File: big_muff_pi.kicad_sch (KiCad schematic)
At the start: 63 parts, among them J1 NMJ6HHD2, J2 NMJ6HHD2, Q1 MMBT5551, Q2 MMBT5551, Q3 MMBT5551, Q4 MMBT5551, Q5 MMBT5551, SW1 SW_DPDT_x2

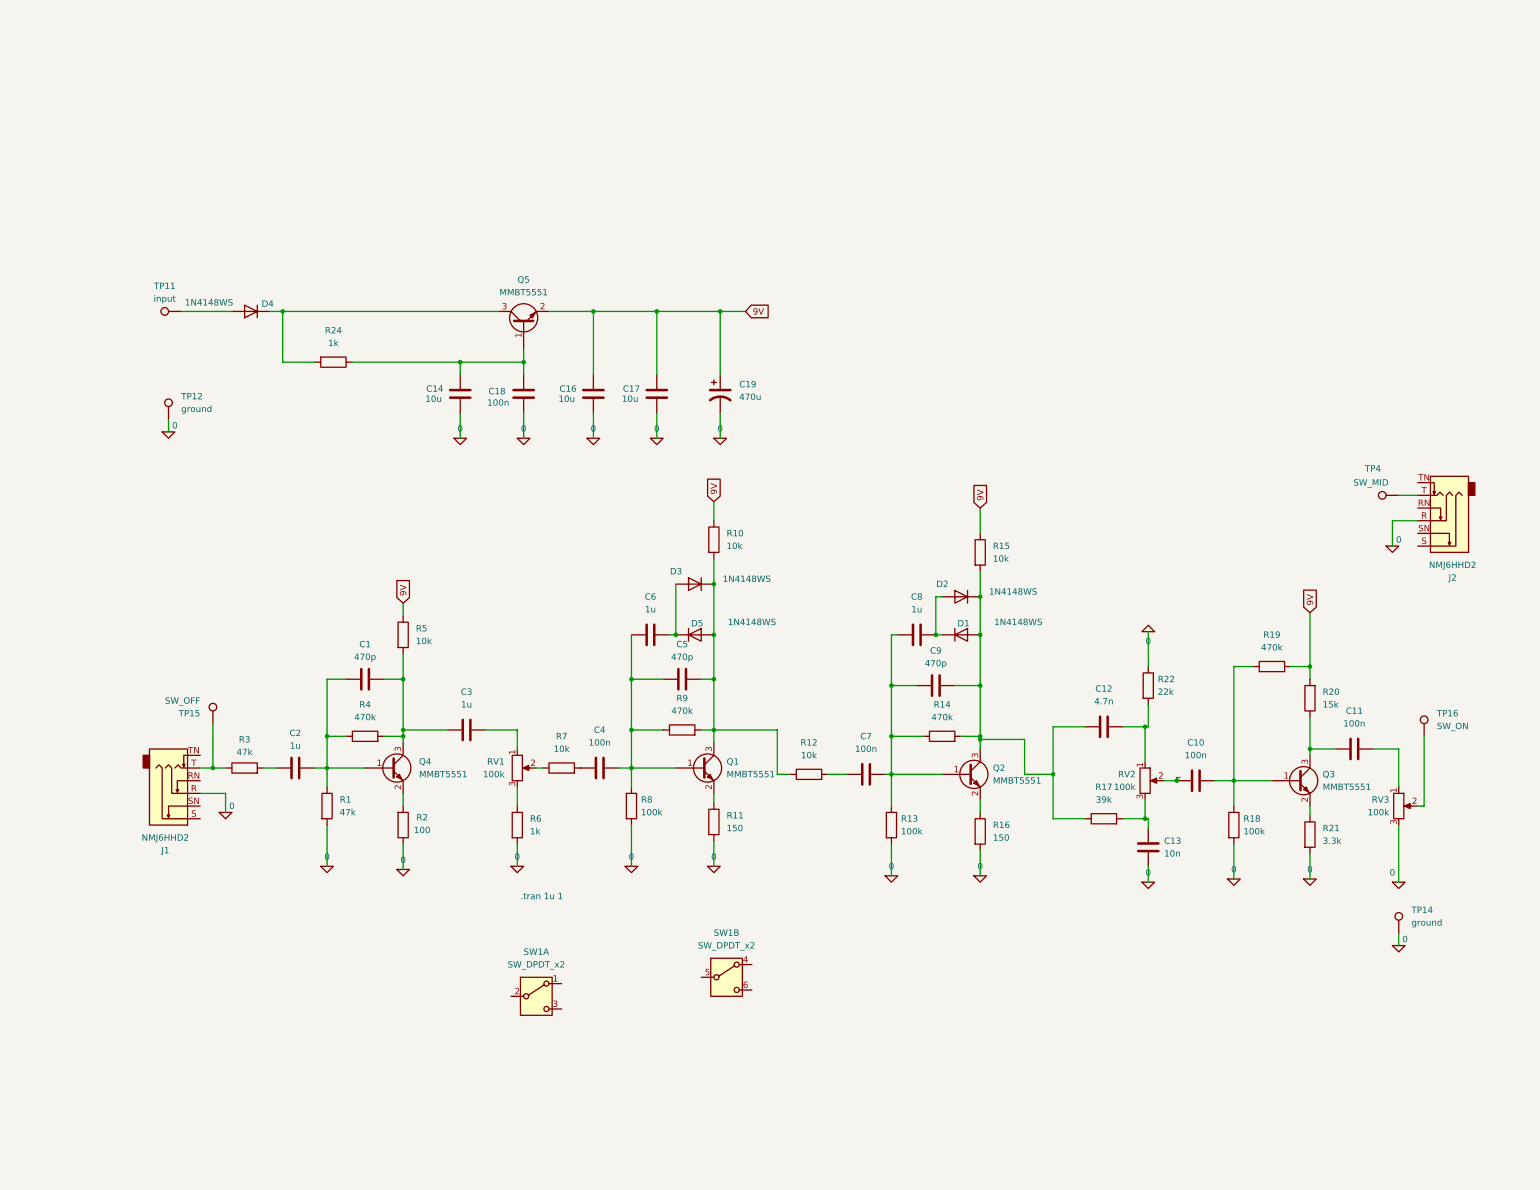
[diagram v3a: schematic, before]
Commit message: 3D bodies
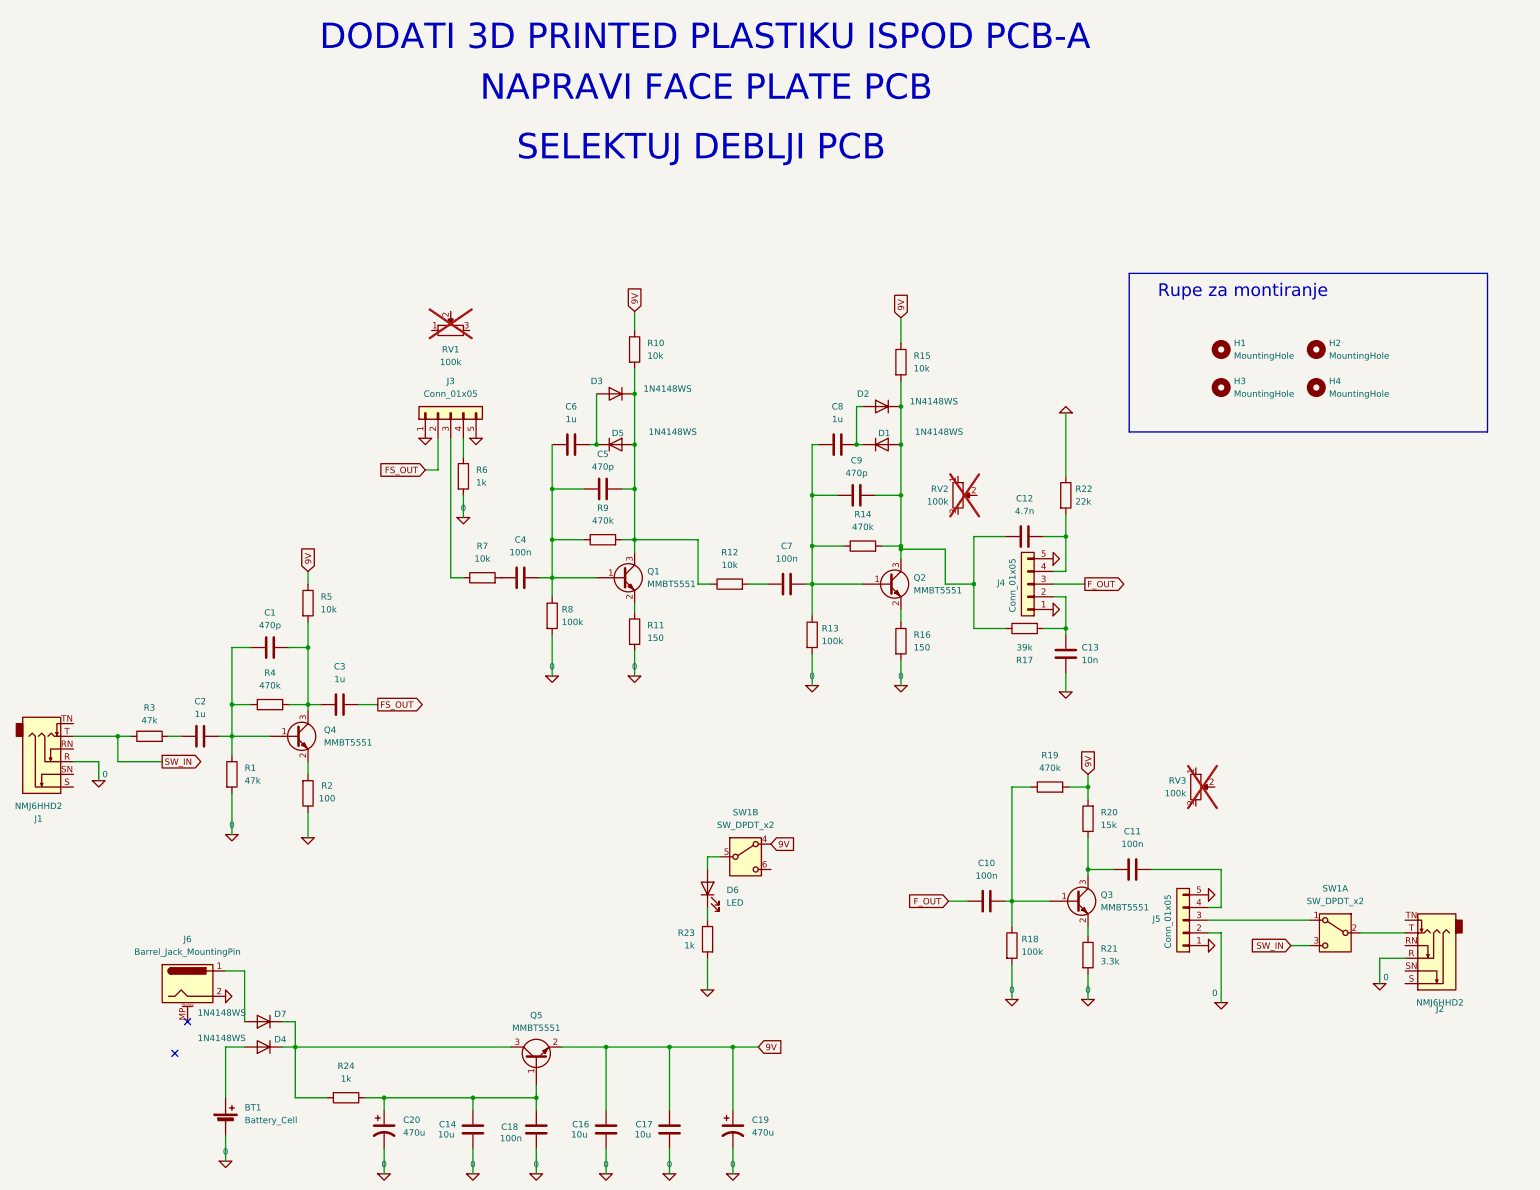
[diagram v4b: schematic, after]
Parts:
- removed TP11: input, TestPoint:TestPoint_THTPad_2.5x2.5mm_Drill1.2mm, symbol Connector:TestPoint
- removed TP12, TP14: ground, TestPoint:TestPoint_THTPad_2.5x2.5mm_Drill1.2mm, symbol Connector:TestPoint
- removed TP15: SW_OFF, TestPoint:TestPoint_THTPad_2.5x2.5mm_Drill1.2mm, symbol Connector:TestPoint
- removed TP16: SW_ON, TestPoint:TestPoint_THTPad_2.5x2.5mm_Drill1.2mm, symbol Connector:TestPoint
- removed TP4: SW_MID, TestPoint:TestPoint_THTPad_2.5x2.5mm_Drill1.2mm, symbol Connector:TestPoint
- added BT1: Battery_Cell, pedale:BatteryHolder_Eagle_12BH611-GR, symbol Device:Battery_Cell
- added C20: 470u, Capacitor_THT:CP_Radial_D8.0mm_P3.50mm, symbol Device:C_Polarized_US
- added D6: LED, LED_THT:LED_D5.0mm, symbol Device:LED
- added D7: 1N4148WS, Diode_SMD:D_SOD-323, symbol Diode:1N4148WS
- added H1, H2, H3, H4: MountingHole, pedale:M3_hole_with_spacer, symbol Mechanical:MountingHole
- added J3, J4, J5: Conn_01x05, Connector_JST:JST_EH_B5B-EH-A_1x05_P2.50mm_Vertical, symbol Connector_Generic:Conn_01x05
- added J6: Barrel_Jack_MountingPin, Connector_BarrelJack:BarrelJack_GCT_DCJ200-10-A_Horizontal, symbol Connector:Barrel_Jack_MountingPin
- added R23: 1k, Resistor_SMD:R_0603_1608Metric_Pad0.98x0.95mm_HandSolder, symbol Device:R
- RV1, RV2, RV3: now not fitted
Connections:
- net 0: now also BT1.2 (-), C20.2, J3.1 (Pin_1), J3.5 (Pin_5), J4.1 (Pin_1), J4.5 (Pin_5), J5.1 (Pin_1), J5.2 (Pin_2), J5.5 (Pin_5), J6.2, R23.2; no longer RV3.3
- net 9V: now also SW1.4 (A)
- net at D4.1 (K), Q5.3 (C), R24.2: now also D7.1 (K)
- net at D4.2 (A): now also BT1.1 (+)
- net at C12.2, R22.2: now also J4.4 (Pin_4); no longer RV2.1
- net at C14.1, C18.2, Q5.1 (B)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: now also C20.1
- net SW_IN: now reaches J1.T, R3.1
- net SW_IN: now also SW1.3 (C)
- net at C13.2, R17.2: now also J4.2 (Pin_2); no longer RV2.3
- net at RV1.1: no longer C3.2
- net at R7.1: now also J3.3 (Pin_3); no longer RV1.2
- net at R6.1: now also J3.4 (Pin_4); no longer RV1.3
- net at J2.T: now also SW1.2 (B)
- net at RV2.2: no longer C10.1
- net at RV3.1: no longer C11.2
- net at SW1.1 (A): now also J5.3 (Pin_3)
- net at SW1.5 (B): now also D6.2 (A)
- new net: D6.1 (K), R23.1
- new net: C11.2, J5.4 (Pin_4)
- new net: D7.2 (A), J6.1
- new net FS_OUT: C3.2, J3.2 (Pin_2)
- new net F_OUT: C10.1, J4.3 (Pin_3)
- no-connect marks 0 -> 2
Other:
- note added: "DODATI 3D PRINTED PLASTIKU ISPOD PCB-A"
- note added: "NAPRAVI FACE PLATE PCB"
- note added: "Rupe za montiranje"
- note added: "SELEKTUJ DEBLJI PCB"
- note removed: ".tran 1u 1"
- moved on the sheet: C1, C10, C11, C12, C13, C14, C16, C17, C18, C19, C2, C3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
